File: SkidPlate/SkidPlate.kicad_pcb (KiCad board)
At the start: 2 copper layers, 100.8 x 56.1 mm, 30 parts, among them J11 XT30UPB-M, J12 XT30UPB-M, J13 XT30UPB-M, J14 XT30UPB-M, J3 JST_BM03B-GHS-TBT, J4 JST_BM04B-GHS-TBT, J5 JST_BM04B-GHS-TBT, J6 JST_BM04B-GHS-TBT, J7 JST_BM04B-GHS-TBT, U1 AMS1117-3.3, U2 LSM6DSOX

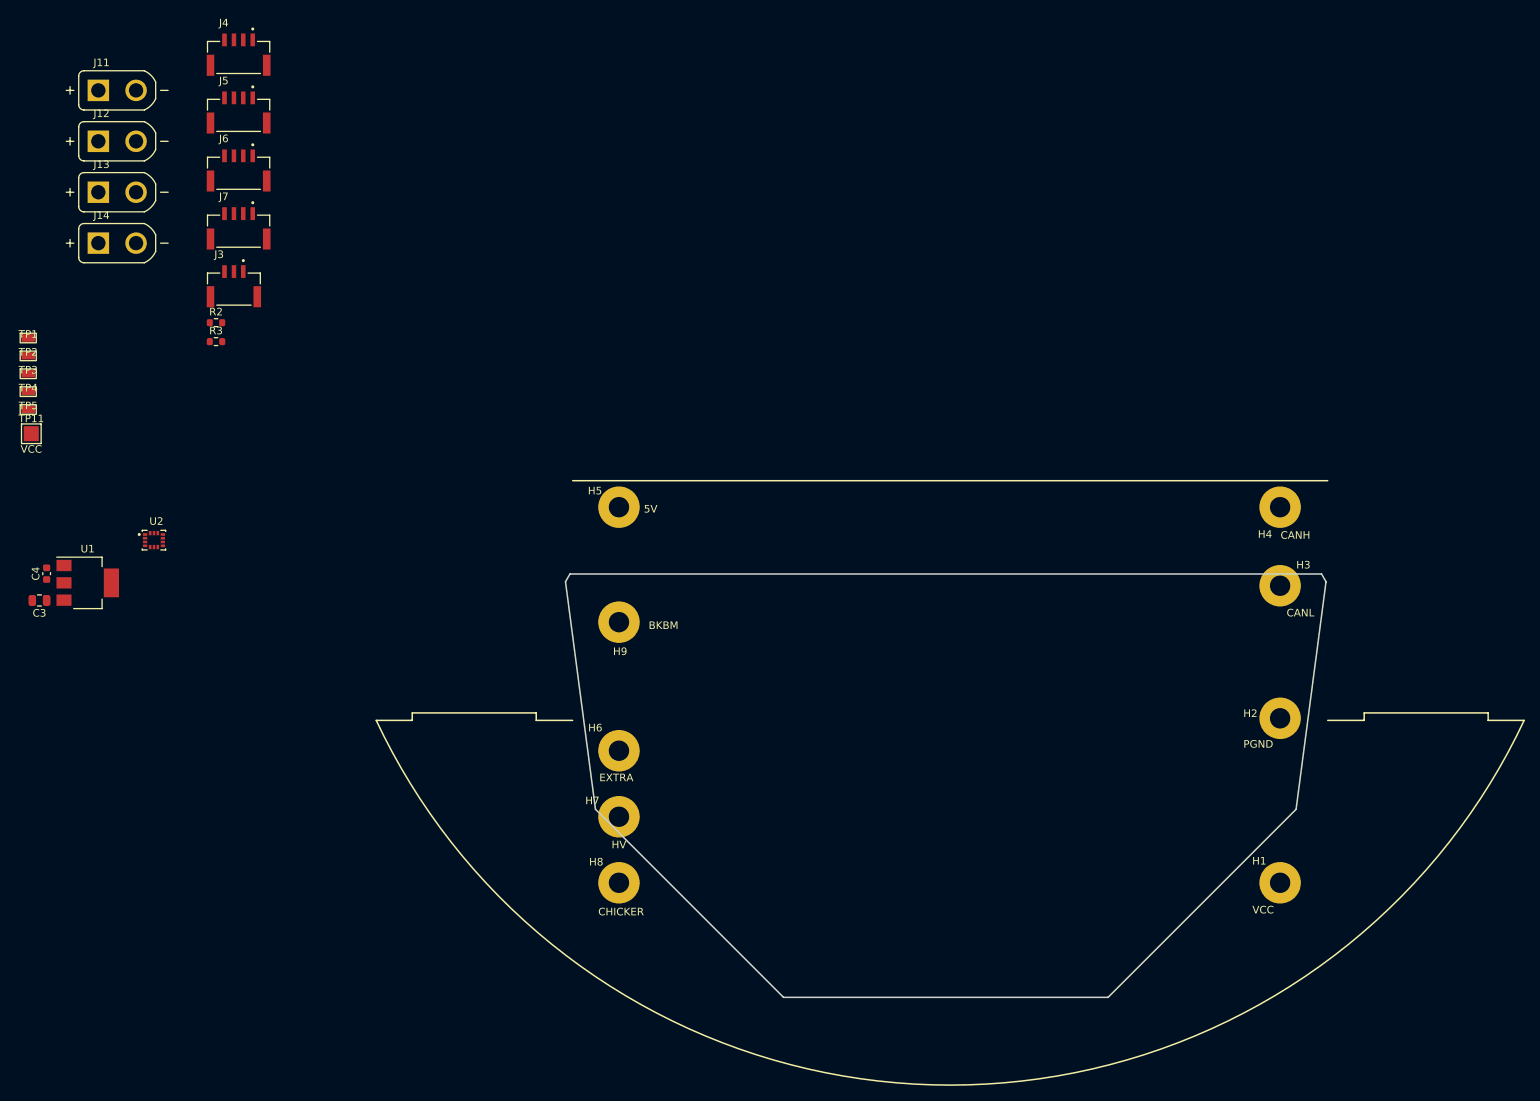
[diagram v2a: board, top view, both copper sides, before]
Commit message: skidplate
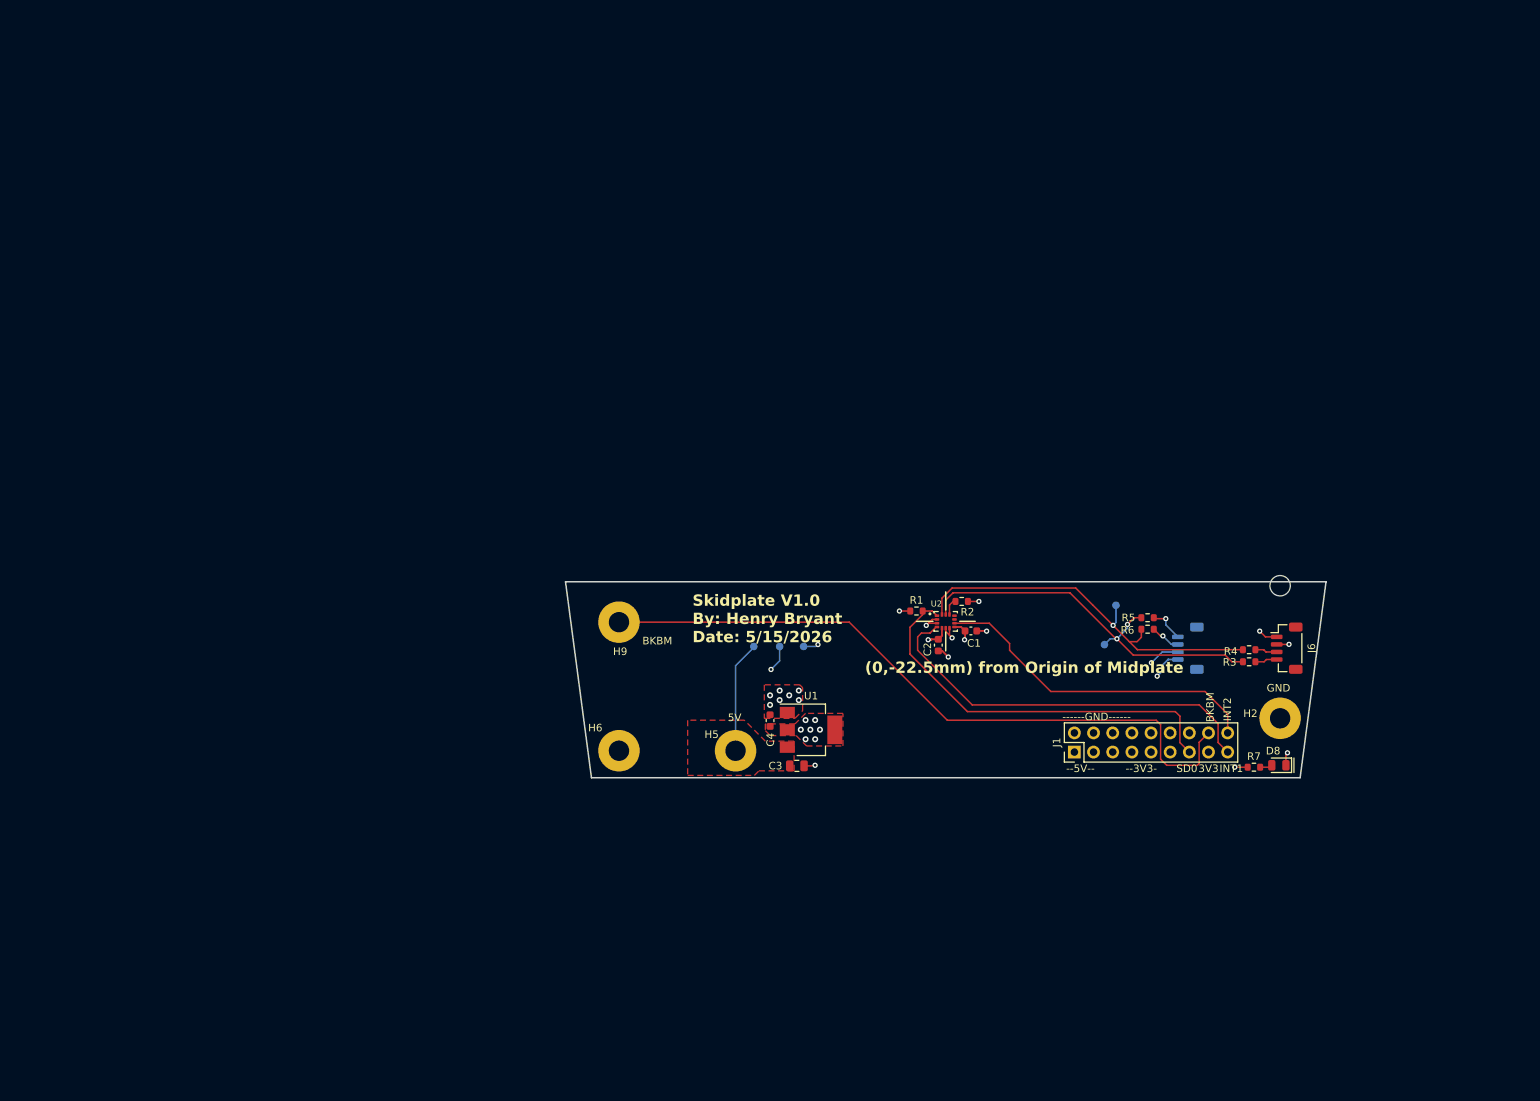
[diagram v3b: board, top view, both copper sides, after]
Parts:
- removed H1: VCC, bots:MountingHole_2.7mm_M2.5_DIN965_Pad
- removed H3: CANL, bots:MountingHole_2.7mm_M2.5_DIN965_Pad
- removed H4: CANH, bots:MountingHole_2.7mm_M2.5_DIN965_Pad
- removed H7: HV, bots:MountingHole_2.7mm_M2.5_DIN965_Pad
- removed H8: CHICKER, bots:MountingHole_2.7mm_M2.5_DIN965_Pad
- removed J11, J12, J13, J14: XT30UPB-M, bots:AMASS_XT30UPB-M
- removed J3: JST_BM03B-GHS-TBT, bots:JST_BM03B-GHS-TBT
- removed J4, J5: JST_BM04B-GHS-TBT, bots:JST_BM04B-GHS-TBT
- removed TP11: VCC, bots:TestPoint_Pad_2.0x2.0mm
- added C1: 0.1u, bots:C_0603_1608Metric, F.Cu at (154.4, 108.8)
- added C2: 0.1u, bots:C_0603_1608Metric, F.Cu at (150.1, 110.7)
- added D8: LED, bots:LED_0805_2012Metric, F.Cu at (195.2, 126.6)
- added J1: Conn_02x09_Counter_Clockwise, bots:PinHeader_2x09_P2.54mm_Vertical, F.Cu at (168.1, 124.9)
- added R1: R_10k, bots:R_0603_1608Metric, F.Cu at (147.2, 106.2)
- added R4: 0R, bots:R_0603_1608Metric, F.Cu at (191.3, 111.3)
- added R5: 0R, bots:R_0603_1608Metric, F.Cu at (177.8, 107.1)
- added R6: 0R, bots:R_0603_1608Metric, F.Cu at (177.8, 108.6)
- added R7: 2k, bots:R_0603_1608Metric, F.Cu at (191.9, 126.9)
- added REF**: MountingHole_No_copper_M2.5, bots:MountingHole_No_copper_M2.5, F.Cu at (195.4, 102.8)
- J6: value JST_BM04B-GHS-TBT -> STEMMA_QT; footprint bots:JST_BM04B-GHS-TBT -> bots:JST_SH_BM04B-SRSS-TB_1x04-1MP_P1.00mm_Vertical
- J7: value JST_BM04B-GHS-TBT -> STEMMA_QT; footprint bots:JST_BM04B-GHS-TBT -> bots:JST_SH_BM04B-SRSS-TB_1x04-1MP_P1.00mm_Vertical; moved to B.Cu
- R2: value 20k -> R_10k; footprint Resistor_SMD:R_0603_1608Metric -> bots:R_0603_1608Metric
- R3: value 10k -> 0R; footprint Resistor_SMD:R_0603_1608Metric -> bots:R_0603_1608Metric
- TP1: value SI -> 5V; footprint bots:pad_0603 -> bots:TestPoint_Pad_D1.0mm; moved to B.Cu
- TP2: value SI -> 3v3; footprint bots:pad_0603 -> bots:TestPoint_Pad_D1.0mm; moved to B.Cu
- TP3: value SI -> GND; footprint bots:pad_0603 -> bots:TestPoint_Pad_D1.0mm; moved to B.Cu
- TP4: value SI -> SCL; footprint bots:pad_0603 -> bots:TestPoint_Pad_D1.0mm; moved to B.Cu
- TP5: value SI -> SDA; footprint bots:pad_0603 -> bots:TestPoint_Pad_D1.0mm; moved to B.Cu
- U2: footprint bots:PQFN50P300X250X86-14N -> bots:PQFN50P250X300X86-14N
- moved J6 152.1 mm to (196.2, 111.1), turned to -90 degrees
- moved TP4 146.5 mm to (172.1, 110.6), turned to 180 degrees
- moved TP5 146.5 mm to (173.6, 105.4), turned to 180 degrees
- moved R3 143.4 mm to (191.3, 112.9)
- moved J7 137.0 mm to (183.1, 111.1), turned to 90 degrees
- moved TP2 109.7 mm to (132.2, 110.9), turned to 180 degrees
- moved TP3 106.0 mm to (129.0, 110.9), turned to 180 degrees
- moved R2 105.5 mm to (153.2, 104.9), turned to 180 degrees
- moved U2 105.5 mm to (151.0, 107.5)
- moved TP1 104.5 mm to (125.6, 110.9), turned to 180 degrees
- moved C3 102.8 mm to (131.3, 126.7), turned to 0 degrees
- moved C4 97.8 mm to (127.8, 120.7)
- moved U1 97.8 mm to (133.2, 121.9)
- moved H5 35.8 mm to (123.2, 124.7)
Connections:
- H6 pad 1: EXTRA -> unconnected-(H6-Pad1)
- H9 pad 1: BKBM -> /BKBM
- J6 pad 2: /baseplate/CAN_P -> +3V3
- J6 pad 3: /baseplate/CAN_N -> Net-(J6-Pin_3)
- J6 pad 4: GND -> Net-(J6-Pin_4)
- J7 pad 2: /baseplate/CAN_P -> +3V3
- J7 pad 3: /baseplate/CAN_N -> Net-(J7-Pin_3)
- J7 pad 4: GND -> Net-(J7-Pin_4)
- R2 pad 1: Net-(J3-Pad1) -> +3V3
- R2 pad 2: GND -> /CS
- R3 pad 1: BKBM -> /IMU_SCL
- R3 pad 2: Net-(J3-Pad1) -> Net-(J6-Pin_4)
- U2 pad 1: unconnected-(U2-SDO/SA0-Pad1) -> /SD0
- U2 pad 11: unconnected-(U2-SDO_AUX-Pad11) -> /SD0_AUX
- U2 pad 12: unconnected-(U2-CS-Pad12) -> /CS
- U2 pad 13: IMU_SCL -> /IMU_SCL
- U2 pad 14: IMU_SDA -> /IMU_SDA
- U2 pad 4: unconnected-(U2-INT1-Pad4) -> /INT1
- U2 pad 5: unconnected-(U2-VDDIO-Pad5) -> +3V3
- U2 pad 9: unconnected-(U2-INT2-Pad9) -> /INT2
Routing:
- net /BKBM: track 0.00 -> 92.1 mm
- net /INT1: track 0.00 -> 53.0 mm
- net /SD0: track 0.00 -> 53.0 mm
- net /IMU_SCL: track 0.00 -> 52.1 mm, vias 0 -> 2
- net /IMU_SDA: track 0.00 -> 51.7 mm, vias 0 -> 1
- net /INT2: track 0.00 -> 44.2 mm
- net GND: track 0.00 -> 22.7 mm, vias 0 -> 16
- net +3V3: track 0.00 -> 18.2 mm, vias 0 -> 15
- net +5V: track 0.00 -> 15.2 mm
- net Net-(J7-Pin_4): track 0.00 -> 4.71 mm, vias 0 -> 1
- net Net-(J7-Pin_3): track 0.00 -> 4.02 mm, vias 0 -> 1
- net Net-(J6-Pin_4): track 0.00 -> 2.95 mm
- net Net-(J6-Pin_3): track 0.00 -> 2.95 mm
- net /CS: track 0.00 -> 2.25 mm
- net /3V3_DIO: track 0.00 -> 1.64 mm
- added copper zone on F.Cu, net +3V3
- added copper zone on In2.Cu, net +3V3
- added copper zone on F.Cu, net +5V
- added copper zone on In2.Cu, net +5V
- added copper zone on F.Cu, net GND
- added copper zone on In1.Cu, net GND
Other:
- board size 100.8 x 56.1 mm -> 100.8 x 26 mm
- copper layers 2 -> 4
- board text added: "(0,-22.5mm) from Origin of Midplate"
- board text added: "(0,0) Origin of Midplate"
- board text added: "------GND------"
- board text added: "--3V3-"
- board text added: "--5V--"
- board text added: "3V3"
- board text added: "5V"
- board text added: "BKBM"
- board text added: "GND"
- board text added: "INT1"
- board text added: "INT2"
- board text added: "SD0"
- board text added: "Skidplate V1.0 By: Henry Bryant Date: 5/15/2026"

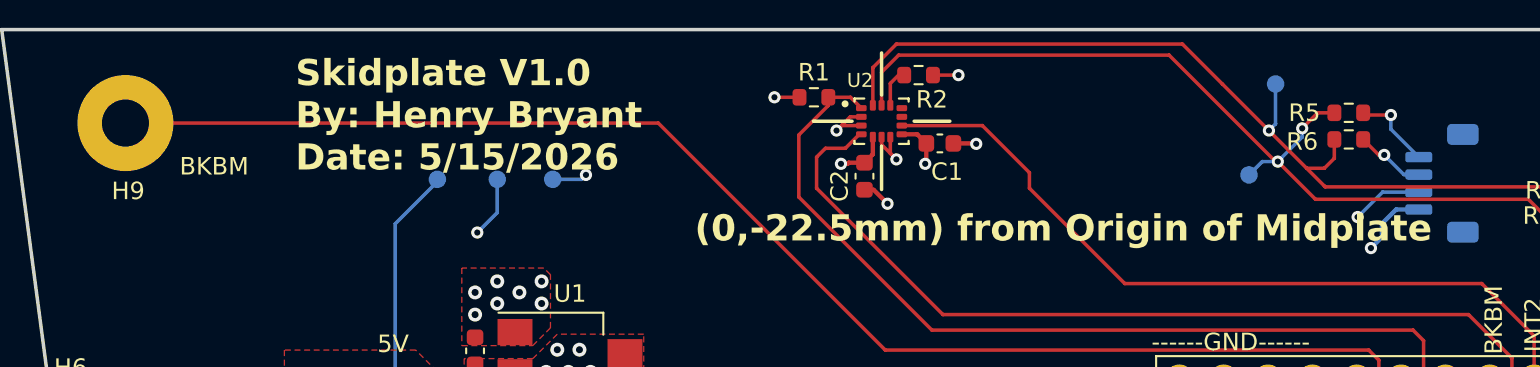
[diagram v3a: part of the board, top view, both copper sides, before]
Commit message: skidplate, then realized its pointless
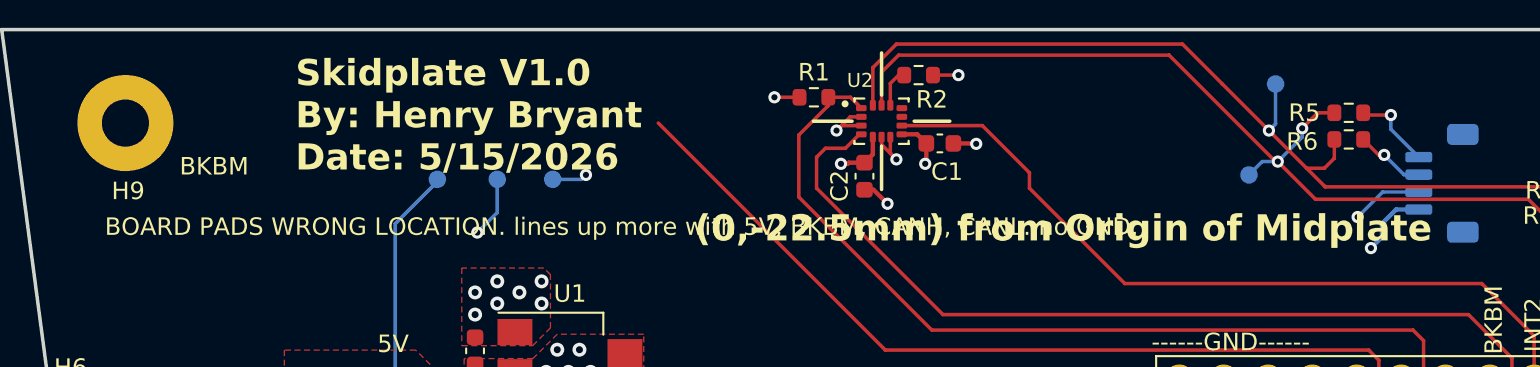
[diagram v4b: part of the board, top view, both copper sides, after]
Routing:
- net /BKBM: track 92.1 -> 61.6 mm
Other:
- board text added: "BOARD PADS WRONG LOCATION. lines up more with 5V, BKBM, CANH, CANL. no GND."
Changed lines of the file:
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@@
 		(layer "Edge.Cuts")
+	)
+	(gr_text "BOARD PADS WRONG LOCATION. lines up more with 5V, BKBM, CANH, CANL. no GND. "
+		(at 106.553 114.173 0)
+		(layer "F.SilkS")
+		(effects
+			(font
+				(size 1 1)
+				(thickness 0.1)
+			)
+			(justify left bottom)
+		)
 	)
 	(gr_text "------GND------"
@@
 		(width 0.2032)
 		(layer "F.Cu")
-		(net "/BKBM")
-	)
-	(segment
-		(start 107.736318 107.648681)
-		(end 138.255681 107.648681)
-		(width 0.2032)
-		(layer "F.Cu")

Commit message: skidplate done
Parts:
- removed H6: EXTRA, bots:MountingHole_2.7mm_M2.5_DIN965_Pad
- removed H9: BKBM, bots:MountingHole_2.7mm_M2.5_DIN965_Pad
- removed REF**: MountingHole_No_copper_M2.5, bots:MountingHole_No_copper_M2.5
- added H1: RPI, bots:MountingHole_2.7mm_M2.5_DIN965_Pad, F.Cu at (107.7, 107.6)
- added H3: CANH, bots:MountingHole_2.7mm_M2.5_DIN965_Pad, F.Cu at (195.4, 118.3)
- moved H5 45.3 mm to (150.9, 128.7)
- moved H2 16.7 mm to (107.7, 118.3)
- moved C4 13.8 mm to (115.3, 114.7)
- moved C3 13.8 mm to (118.9, 120.7)
- moved U1 13.8 mm to (120.8, 115.9)
- moved R7 10.0 mm to (182.8, 130.9)
- moved D8 10.0 mm to (186.1, 130.7)
- moved C1 3.40 mm to (154.4, 112.2)
- moved C2 3.40 mm to (150.1, 114.1)
- moved R1 3.40 mm to (147.2, 109.6)
- moved R2 3.40 mm to (153.2, 108.3)
- moved U2 3.40 mm to (151.0, 110.9)
- moved J7 1.78 mm to (184.4, 109.9)
- moved R3 1.24 mm to (191.3, 111.7)
- moved R4 1.24 mm to (191.3, 110.1)
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- renumbered H5 to H2, H2 to H5
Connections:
- J1 pad 11: /BKBM -> +3V3
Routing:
- net /BKBM: track 61.6 -> 0.00 mm
- net GND: track 22.7 -> 19.8 mm
- net /INT2: track 44.2 -> 42.3 mm
- net +3V3: track 18.2 -> 16.4 mm
- net /INT1: track 53.0 -> 51.6 mm
- net /SD0: track 53.0 -> 51.6 mm
- net /IMU_SCL: track 52.1 -> 51.2 mm
- net Net-(J7-Pin_3): track 4.02 -> 4.87 mm
- net +5V: track 15.2 -> 14.5 mm, vias 0 -> 1
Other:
- board size 100.8 x 26 mm -> 99.1 x 30.1 mm
- board text added: "Skidplate V1.0 By: Henry Bryant Date: 5/16/2026"
- board text removed: "(0,-22.5mm) from Origin of Midplate"
- board text removed: "BKBM"
- board text removed: "BOARD PADS WRONG LOCATION. lines up more with 5V, BKBM, CANH, CANL. no GND."
- board text removed: "Skidplate V1.0 By: Henry Bryant Date: 5/15/2026"

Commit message: skidplate and midplate
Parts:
- moved H5 10.2 mm to (140.7, 128.0)
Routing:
- net +5V: track 14.5 -> 9.71 mm
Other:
- board size 99.1 x 30.1 mm -> 97.2 x 29.1 mm
